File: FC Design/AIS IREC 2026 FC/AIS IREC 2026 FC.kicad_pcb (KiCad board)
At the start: 4 copper layers, 80 x 40 mm, 50 parts, among them IC1 ADXL314WBCPZ-RL, IC2 MT29F8G08ABACAWP-IT_C_TR, J1 USB4216-03-A, J2 EBAA-02-C, J3 Conn_01x08, J4 EBAA-02-C, J5 EBAA-02-C, Q1 MMBT3906-TP, Q2 DMN2008LFU-7, Q3 DMN2008LFU-7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

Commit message: Updates to pcb
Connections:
- C29 pad 1: Noise Capacitors 1.8V -> 1.8V
- U6 pad 15: Noise Capacitors 1.8V -> 1.8V
- U6 pad 26: Noise Capacitors 1.8V -> 1.8V
- U6 pad 29: Noise Capacitors 1.8V -> 1.8V
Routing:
- net Capacitor Ground: track 0.00 -> 81.1 mm, vias 4 -> 19
- net 3.3V: track 0.00 -> 51.7 mm, vias 0 -> 12
- net 1.8V: track 0.00 -> 39.4 mm, vias 0 -> 5
- net Vsrc: track 0.00 -> 14.2 mm, vias 0 -> 1
- net MAIN OUT: track 0.00 -> 8.31 mm
- net DROGUE OUT: track 0.00 -> 5.83 mm
- net Net-(LS1-+): track 0.00 -> 3.29 mm
- net OSC_CLK: track 0.00 -> 3.05 mm, vias 0 -> 1
- net Net-(J1-CC1): track 0.00 -> 2.38 mm
- net VCAP: track 0.00 -> 1.91 mm
- net Net-(U1-NRST): track 0.00 -> 1.64 mm

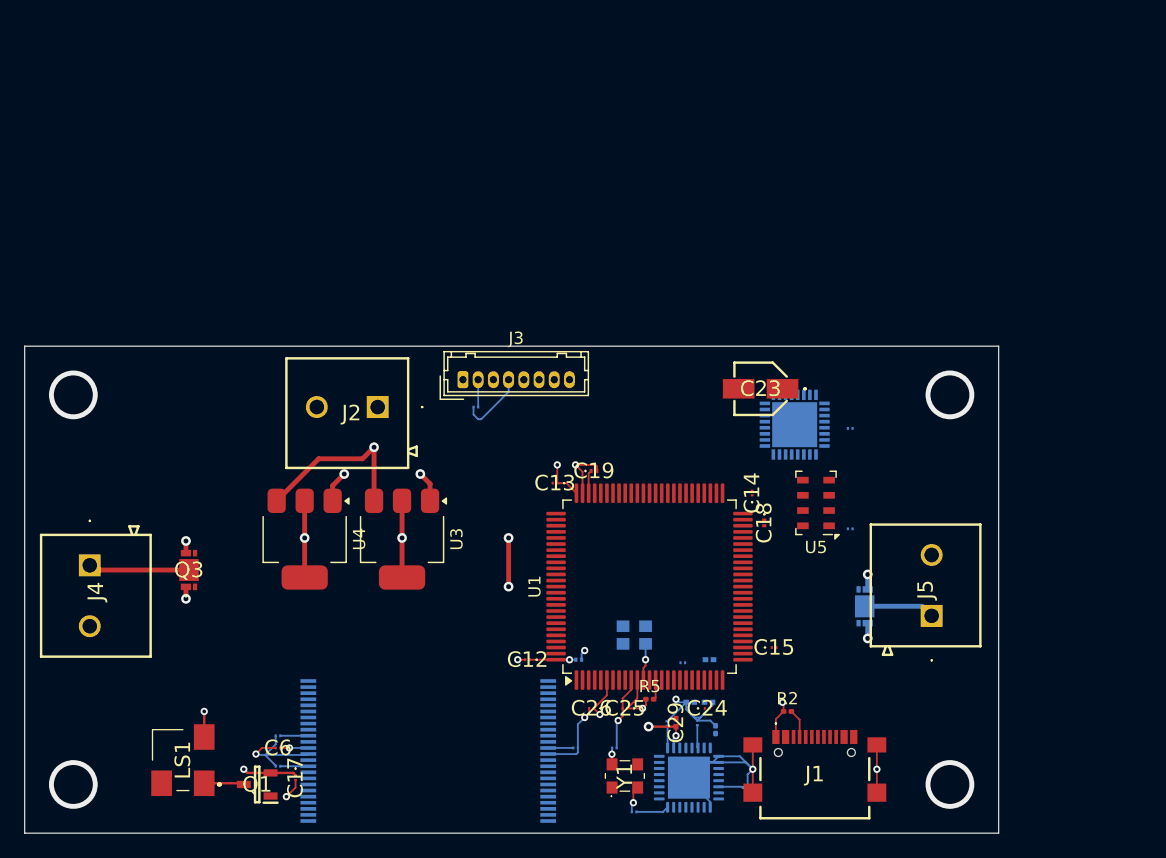
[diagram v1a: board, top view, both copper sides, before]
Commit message: Added PCB layout
Layout is 48% smaller than AV bay was designed to hold, so no issues, space left because I'm lazy. Allows for further improvement in subsequent years.
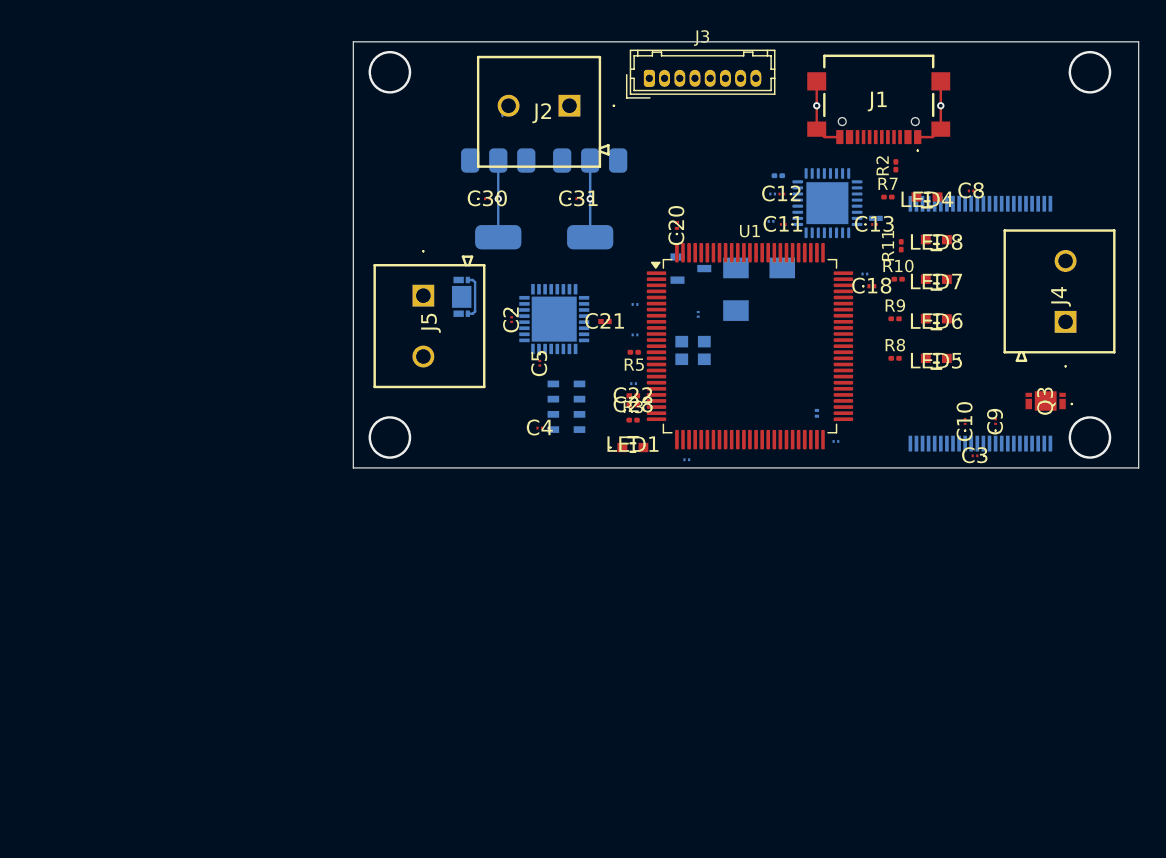
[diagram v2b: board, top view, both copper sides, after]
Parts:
- removed C23: 10uF, SamacSys_Parts:10SVPS10M
- removed C24, C25: 100nF, SamacSys_Parts:GRM022C81C222KE01L
- removed Y1: DSC1001CL5-060.0000, SamacSys_Parts:DSC6183CI2A032K768
- added C30: 100nF, SamacSys_Parts:GRM022C81C222KE01L, F.Cu at (158.0, 37.9)
- added C31: 100nF, SamacSys_Parts:GRM022C81C222KE01L, F.Cu at (165.5, 37.9)
- added LED1: 598-8D91-127F, SamacSys_Parts:5988D91127F, F.Cu at (170.0, 58.3)
- added LED4: 598-8D91-127F, SamacSys_Parts:5988D91127F, F.Cu at (194.1, 37.8)
- added LED5: 598-8D91-127F, SamacSys_Parts:5988D91127F, F.Cu at (194.9, 51.0)
- added LED6: 598-8D91-127F, SamacSys_Parts:5988D91127F, F.Cu at (194.9, 47.8)
- added LED7: 598-8D91-127F, SamacSys_Parts:5988D91127F, F.Cu at (194.9, 44.5)
- added LED8: 598-8D91-127F, SamacSys_Parts:5988D91127F, F.Cu at (194.9, 41.2)
- added R10: 10KR, Resistor_SMD:R_0201_0603Metric, F.Cu at (191.8, 44.5)
- added R11: 10KR, Resistor_SMD:R_0201_0603Metric, F.Cu at (192.0, 41.8)
- added R3: 10KR, Resistor_SMD:R_0201_0603Metric, F.Cu at (170.0, 56.1)
- added R7: 10KR, Resistor_SMD:R_0201_0603Metric, F.Cu at (190.9, 37.8)
- added R8: 10KR, Resistor_SMD:R_0201_0603Metric, F.Cu at (191.5, 51.0)
- added R9: 10KR, Resistor_SMD:R_0201_0603Metric, F.Cu at (191.5, 47.8)
- C10, C11, C2, C20, C21, C22, C28, C3, C4, C5, C8, C9: moved to F.Cu
- C14, C15, C17, C19, C26, C29, C6, LS1, Q1, U3, U4, U5: moved to B.Cu
- moved J4 82.6 mm to (205.5, 48.0), turned to 90 degrees
- moved Q3 71.7 mm to (203.9, 54.5), turned to 90 degrees
- moved C7 62.9 mm to (189.0, 44.1), turned to 0 degrees
- moved LS1 61.1 mm to (180.3, 45.3), turned to 0 degrees
- moved IC2 57.3 mm to (198.5, 48.1), turned to -90 degrees
- moved J1 56.2 mm to (190.2, 29.5), turned to 180 degrees
- moved Q1 55.4 mm to (174.7, 43.6), turned to 0 degrees
- moved C8 52.4 mm to (197.8, 37.2), turned to 180 degrees
- moved C17 50.4 mm to (175.3, 47.4), turned to 90 degrees
- moved J5 49.3 mm to (152.8, 45.9), turned to -90 degrees
- moved U6 48.5 mm to (185.9, 38.2), turned to -90 degrees
- moved R1 45.8 mm to (181.9, 36.0), turned to 0 degrees
- moved R2 45.7 mm to (191.6, 35.2), turned to 90 degrees
- moved C11 45.2 mm to (182.3, 40.0), turned to 180 degrees
- moved C26 44.8 mm to (181.4, 37.5)
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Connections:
- C1 pad 2: Capacitor Ground -> GND
- C10 pad 2: Capacitor Ground -> GND
- C11 pad 2: Capacitor Ground -> GND
- C12 pad 2: Capacitor Ground -> GND
- C13 pad 2: Capacitor Ground -> GND
- C14 pad 2: Capacitor Ground -> GND
- C15 pad 2: Capacitor Ground -> GND
- C16 pad 2: Capacitor Ground -> GND
- C17 pad 2: Capacitor Ground -> GND
- C18 pad 2: Capacitor Ground -> GND
- C19 pad 2: Capacitor Ground -> GND
- C2 pad 2: Capacitor Ground -> GND
- C20 pad 2: Capacitor Ground -> GND
- C21 pad 2: Capacitor Ground -> GND
- C22 pad 2: Capacitor Ground -> GND
- C26 pad 1: 3.3V -> 1.8V
- C26 pad 2: Capacitor Ground -> GND
- C27 pad 1: 3.3V -> 1.8V
- C27 pad 2: Capacitor Ground -> GND
- C28 pad 2: Capacitor Ground -> GND
- C29 pad 2: Capacitor Ground -> GND
- C3 pad 2: Capacitor Ground -> GND
- C4 pad 2: Capacitor Ground -> GND
- C5 pad 2: Capacitor Ground -> GND
- C6 pad 2: Capacitor Ground -> GND
- C7 pad 2: Capacitor Ground -> GND
- C8 pad 2: Capacitor Ground -> GND
- C9 pad 2: Capacitor Ground -> GND
- IC1 pad 1: Capacitor Ground -> GND
- IC1 pad 3: Capacitor Ground -> GND
- IC1 pad 33: Capacitor Ground -> GND
- IC1 pad 4: Capacitor Ground -> GND
- IC2 pad 13: Capacitor Ground -> GND
- IC2 pad 25: Capacitor Ground -> GND
- IC2 pad 36: Capacitor Ground -> GND
- IC2 pad 48: Capacitor Ground -> GND
- J1 pad A1: Capacitor Ground -> GND
- J1 pad B1: Capacitor Ground -> GND
- J1 pad G1: Capacitor Ground -> GND
- J1 pad G2: Capacitor Ground -> GND
- J1 pad G3: Capacitor Ground -> GND
- J1 pad G4: Capacitor Ground -> GND
- J2 pad 2: Capacitor Ground -> GND
- J3 pad 3: 3.3V -> Vsrc
- J3 pad 4: Capacitor Ground -> GND
- J4 pad 2: Capacitor Ground -> GND
- J5 pad 2: Capacitor Ground -> GND
- LS1 pad 2: Capacitor Ground -> GND
- Q2 pad 1: 3.3V -> Vsrc
- Q2 pad 4: 3.3V -> Vsrc
- Q3 pad 1: 3.3V -> Vsrc
- Q3 pad 4: 3.3V -> Vsrc
- R1 pad 1: Net-(U6-RBIAS) -> GND
- R1 pad 2: Capacitor Ground -> Net-(U6-RBIAS)
- R2 pad 1: Capacitor Ground -> GND
- R5 pad 1: 3.3V -> Net-(U1-NRST)
- R5 pad 2: Net-(U1-NRST) -> 3.3V
- U1 pad 10: Capacitor Ground -> GND
- U1 pad 20: Capacitor Ground -> GND
- U1 pad 27: Capacitor Ground -> GND
- U1 pad 3: unconnected-(U1-PE4-Pad3) -> INDICATOR 1
- U1 pad 38: unconnected-(U1-PE7-Pad38) -> INDICATOR 4
- U1 pad 4: unconnected-(U1-PE5-Pad4) -> INDICATOR 2
- U1 pad 5: unconnected-(U1-PE6-Pad5) -> INDICATOR 3
- U1 pad 74: Capacitor Ground -> GND
- U2 pad 2: Capacitor Ground -> GND
- U3 pad 1: Capacitor Ground -> GND
- U4 pad 1: Capacitor Ground -> GND
- U5 pad 2: Capacitor Ground -> GND
- U5 pad 3: Capacitor Ground -> GND
- U6 pad 1: Capacitor Ground -> GND
- U6 pad 2: Capacitor Ground -> GND
- U6 pad 33: Capacitor Ground -> GND
- U6 pad 9: Capacitor Ground -> GND
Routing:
- net Capacitor Ground: track 81.1 -> 0.00 mm, vias 19 -> 0
- net 3.3V: track 51.7 -> 6.30 mm, vias 12 -> 1
- net 1.8V: track 39.4 -> 6.30 mm, vias 5 -> 1
- net Vsrc: track 14.2 -> 0.00 mm, vias 1 -> 0
- net GND: track 0.00 -> 13.0 mm, vias 0 -> 2
- net MAIN OUT: track 8.31 -> 0.00 mm
- net DROGUE OUT: track 5.83 -> 0.00 mm
- net DROGUE: track 0.00 -> 3.75 mm
- net Net-(LS1-+): track 3.29 -> 0.00 mm
- net OSC_CLK: track 3.05 -> 0.00 mm, vias 1 -> 0
- net Net-(J1-CC1): track 2.38 -> 0.00 mm
- net VCAP: track 1.91 -> 0.00 mm
- net Net-(U1-NRST): track 1.64 -> 0.00 mm
- net (no net): vias 0 -> 4
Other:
- board size 80 x 40 mm -> 64.5 x 35 mm

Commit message: Fucking hell
All of the routing. All of the fucking routing.
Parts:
- added C23: 100nF, SamacSys_Parts:GRM022C81C222KE01L, B.Cu at (171.5, 42.3)
- C2, C21: moved to B.Cu
- moved C2 30.4 mm to (186.8, 33.5), turned to 0 degrees
- moved C21 7.92 mm to (159.8, 47.8), turned to -90 degrees
- moved C7 0.55 mm to (189.6, 44.1)
- moved U6 0.31 mm to (185.9, 37.9)
- turned C31 to 180 degrees
- turned Q3 to -90 degrees
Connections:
- Q2 pad 1: Vsrc -> 3.3V
- Q2 pad 4: Vsrc -> 3.3V
- Q3 pad 1: Vsrc -> 3.3V
- Q3 pad 4: Vsrc -> 3.3V
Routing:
- net GND: track 13.0 -> 126.5 mm, vias 2 -> 44
- net 3.3V: track 6.30 -> 63.2 mm, vias 1 -> 31
- net MAIN: track 0.00 -> 39.4 mm, vias 0 -> 2
- net USB DIR: track 0.00 -> 38.9 mm, vias 0 -> 2
- net USB NXT: track 0.00 -> 37.3 mm, vias 0 -> 2
- net DP: track 0.00 -> 32.1 mm, vias 0 -> 4
- net USB STP: track 0.00 -> 31.9 mm, vias 0 -> 2
- net WP: track 0.00 -> 30.8 mm, vias 0 -> 1
- net CLK: track 0.00 -> 28.7 mm, vias 0 -> 4
- net DN: track 0.00 -> 28.3 mm, vias 0 -> 2
- net NAND1: track 0.00 -> 28.0 mm, vias 0 -> 5
- net WE: track 0.00 -> 27.9 mm, vias 0 -> 1
- net ALE: track 0.00 -> 27.8 mm, vias 0 -> 1
- net INDICATOR 1: track 0.00 -> 27.0 mm, vias 0 -> 2
- net NAND0: track 0.00 -> 27.0 mm, vias 0 -> 1
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- added copper zone on B.Cu, net 1.8V
- added copper zone on In1.Cu, net 3.3V
- added copper zone on F.Cu, net GND
- added copper zone on In2.Cu, net GND

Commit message: PCB routing changes
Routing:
- net NAND2: track 19.9 -> 28.7 mm
- net NAND0: track 27.0 -> 27.9 mm

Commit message: Changed from usb fs and hs to just usb fs, made appropriate changes
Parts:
- removed C11, C12, C13, C2, C26, C27, C30: 100nF, SamacSys_Parts:GRM022C81C222KE01L
- removed C29: 1uF, SamacSys_Parts:CAPC0603X33N
- removed R1: 12KR, Resistor_SMD:R_0201_0603Metric
- removed U3: AZ1117-1.8, Package_TO_SOT_SMD:SOT-223-3_TabPin2
- removed U6: USB3300-EZK, Package_DFN_QFN:QFN-32-1EP_5x5mm_P0.5mm_EP3.45x3.45mm
- added J6: Conn_01x08, Connector_Hirose:Hirose_DF13-08P-1.25DSA_1x08_P1.25mm_Vertical, F.Cu at (208.0, 32.2)
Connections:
- J1 pad A4: USB VBUS -> unconnected-(J1-VBUS_1-PadA4)
- J1 pad B4: USB VBUS -> unconnected-(J1-VBUS_2-PadB4)
- J3 pad 1: BOOT High -> unconnected-(J3-Pin_1-Pad1)
- J3 pad 2: 3.3V -> unconnected-(J3-Pin_2-Pad2)
- U1 pad 15: USB STP -> unconnected-(U1-PC0-Pad15)
- U1 pad 17: USB DIR -> unconnected-(U1-PC2-Pad17)
- U1 pad 18: USB NXT -> unconnected-(U1-PC3-Pad18)
- U1 pad 26: USB D0 -> unconnected-(U1-PA3-Pad26)
- U1 pad 30: USB CK -> unconnected-(U1-PA5-Pad30)
- U1 pad 35: USB D1 -> unconnected-(U1-PB0-Pad35)
- U1 pad 36: USB D2 -> unconnected-(U1-PB1-Pad36)
- U1 pad 47: USB D3 -> unconnected-(U1-PB10-Pad47)
- U1 pad 48: USB D4 -> unconnected-(U1-PB11-Pad48)
- U1 pad 51: USB D5 -> unconnected-(U1-PB12-Pad51)
- U1 pad 52: USB D6 -> unconnected-(U1-PB13-Pad52)
- U1 pad 67: unconnected-(U1-PA8-Pad67) -> NAND6
- U1 pad 69: NAND6 -> USB ID
- U1 pad 91: USB D7 -> unconnected-(U1-PB5-Pad91)
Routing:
- net USB DIR: track 38.9 -> 0.00 mm, vias 2 -> 0
- net USB NXT: track 37.3 -> 0.00 mm, vias 2 -> 0
- net USB STP: track 31.9 -> 0.00 mm, vias 2 -> 0
- net GND: track 126.5 -> 97.2 mm, vias 44 -> 35
- net USB ID: track 0.00 -> 25.8 mm, vias 0 -> 1
- net 1.8V: track 24.1 -> 0.00 mm, vias 3 -> 0
- net USB D0: track 22.4 -> 0.00 mm, vias 1 -> 0
- net OSC_CLK: track 24.5 -> 2.13 mm, vias 3 -> 1
- net USB D2: track 20.9 -> 0.00 mm, vias 2 -> 0
- net USB D1: track 20.3 -> 0.00 mm, vias 1 -> 0
- net USB D3: track 19.0 -> 0.00 mm, vias 2 -> 0
- net USB D4: track 18.8 -> 0.00 mm, vias 2 -> 0
- net USB D5: track 17.5 -> 0.00 mm, vias 2 -> 0
- net USB D6: track 17.4 -> 0.00 mm, vias 2 -> 0
- net USB D7: track 15.1 -> 0.00 mm, vias 2 -> 0
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- added copper zone on B.Cu, net (none)
- removed copper zone on B.Cu, net 1.8V

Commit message: Got PCB to a state where I'm happy for Logan to look at it before manufacture
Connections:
- J3 pad 3: Vsrc -> 3.3V
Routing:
- net Vsrc: track 16.0 -> 6.66 mm
- net GND: track 97.2 -> 101.1 mm, vias 35 -> 34
- net unconnected-(U1-PB10-Pad47): track 3.36 -> 0.00 mm
- added copper zone on B.Cu, net 3.3V
- removed copper zone on B.Cu, net (none)
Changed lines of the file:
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@@
 		(tags "connector Hirose DF13 vertical")
 		(property "Reference" "J6"
-			(at 4.38 -3.4 360)
+			(at 4.38 -3.4 0)
 			(layer "F.SilkS")
 			(effects
@@
 		)
 		(property "Value" "Conn_01x08"
-			(at 4.38 2.4 360)
+			(at 4.38 2.4 0)
 			(layer "F.Fab")
 			(effects
@@
 		)
 		(fp_text user "${REFERENCE}"
-			(at 4.38 -1.5 360)
+			(at 4.38 -1.5 0)
 			(layer "F.Fab")
 			(effects
@@
 			(layers "*.Cu" "*.Mask")
 			(remove_unused_layers no)
-			(net 77 "Vsrc")
+			(net 2 "3.3V")
 			(pinfunction "Pin_3")
 			(pintype "passive")
@@
 	)
 	(via
-		(at 164.75 32.5)
-		(size 0.6)
-		(drill 0.3)
-		(layers "F.Cu" "B.Cu")
-		(net 1)
-	)
-	(via
 		(at 195.25 30.25)
 		(size 0.6)
@@
 	)
 	(segment
+		(start 164.15 34.75)
+		(end 164.15 34.65)
+		(width 1)
+		(layer "B.Cu")
+		(net 1)
+	)
+	(segment
 		(start 161.075 49.5)
 		(end 161.775 49.5)
@@
 	)
 	(segment
-		(start 164.15 34.75)
-		(end 164.15 33.1)
-		(width 0.2)
-		(layer "B.Cu")
-		(net 1)
-	)
-	(segment
 		(start 169.575 49.075)
 		(end 169.5 49)
@@
 	)
 	(segment
-		(start 164.15 33.1)
-		(end 164.75 32.5)
-		(width 0.2)
-		(layer "B.Cu")
-		(net 1)
-	)
-	(segment
 		(start 161.05 49.525)
 		(end 161.075 49.5)
@@
 	)
 	(segment
+		(start 164.15 34.65)
+		(end 159.75 30.25)
+		(width 1)
+		(layer "B.Cu")
+		(net 1)
+	)
+	(segment
 		(start 185.075 55.276)
 		(end 185.075 54.075)
@@
 	)
 	(segment
-		(start 164.75 31.2)
+		(start 168.75 34.25)
 		(end 164.75 30.25)
-		(width 0.2)
-		(layer "B.Cu")
-		(net 77)
-	)
-	(segment
-		(start 173.81 29.69)
-		(end 173.81 28)
-		(width 0.2)
+		(width 1)
 		(layer "B.Cu")
 		(net 77)
@@
 	(segment
 		(start 168.75 34.75)
-		(end 173.81 29.69)
-		(width 0.2)
-		(layer "B.Cu")
-		(net 77)
-	)
-	(segment
-		(start 168.75 34.75)
-		(end 164.75 30.75)
-		(width 0.2)
+		(end 168.75 34.25)
+		(width 1)
 		(layer "B.Cu")
 		(net 77)
@@
 	)
 	(segment
-		(start 186.374999 45.049265)
-		(end 184 47.424264)
-		(width 0.1)
-		(layer "In2.Cu")
-		(net 104)
-	)
-	(segment
 		(start 173.575 56.875001)
 		(end 173.575 57.675)
@@
 	)
 	(zone
-		(net 0)
-		(net_name "")
+		(net 2)
+		(net_name "3.3V")
 		(layer "B.Cu")
 		(hatch edge 0.5)

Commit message: Generated gerber and drill files for pcb
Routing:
- net NAND2: track 28.7 -> 20.4 mm
- net NAND4: track 16.9 -> 24.4 mm
- net MOSI: track 20.2 -> 22.4 mm
- net NAND7: track 22.2 -> 23.8 mm
- net CLK: track 28.7 -> 30.0 mm
- net unconnected-(U1-PB5-Pad91): track 0.83 -> 0.00 mm
- added copper zone on In2.Cu, net 3.3V
- added copper zone on B.Cu, net GND
- added copper zone on In1.Cu, net GND
- removed copper zone on B.Cu, net 3.3V
- removed copper zone on In1.Cu, net 3.3V
- removed copper zone on In2.Cu, net GND
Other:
- board size 64.5 x 35 mm -> 65.3 x 38 mm
